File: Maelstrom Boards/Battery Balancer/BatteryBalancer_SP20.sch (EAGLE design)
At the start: 84 parts, among them IC3 REG1117, P2 39-30-16, Q1 SPB80P06P, Q10 MOSFET-NCH-AO3404A, Q11 MOSFET-NCH-AO3404A, Q19 FDD4141TO252, Q2 SPB80P06P, Q22 FDD4141TO252, Q3 NMOSFET-D2PAK-7, Q4 310mA/60V/1.6Ω, Q5 NMOSFET-D2PAK-7, Q6 FDD4141TO252, Q7 MOSFET-NCH-AO3404A, Q8 MOSFET-NCH-AO3404A, Q9 MOSFET-NCH-AO3404A

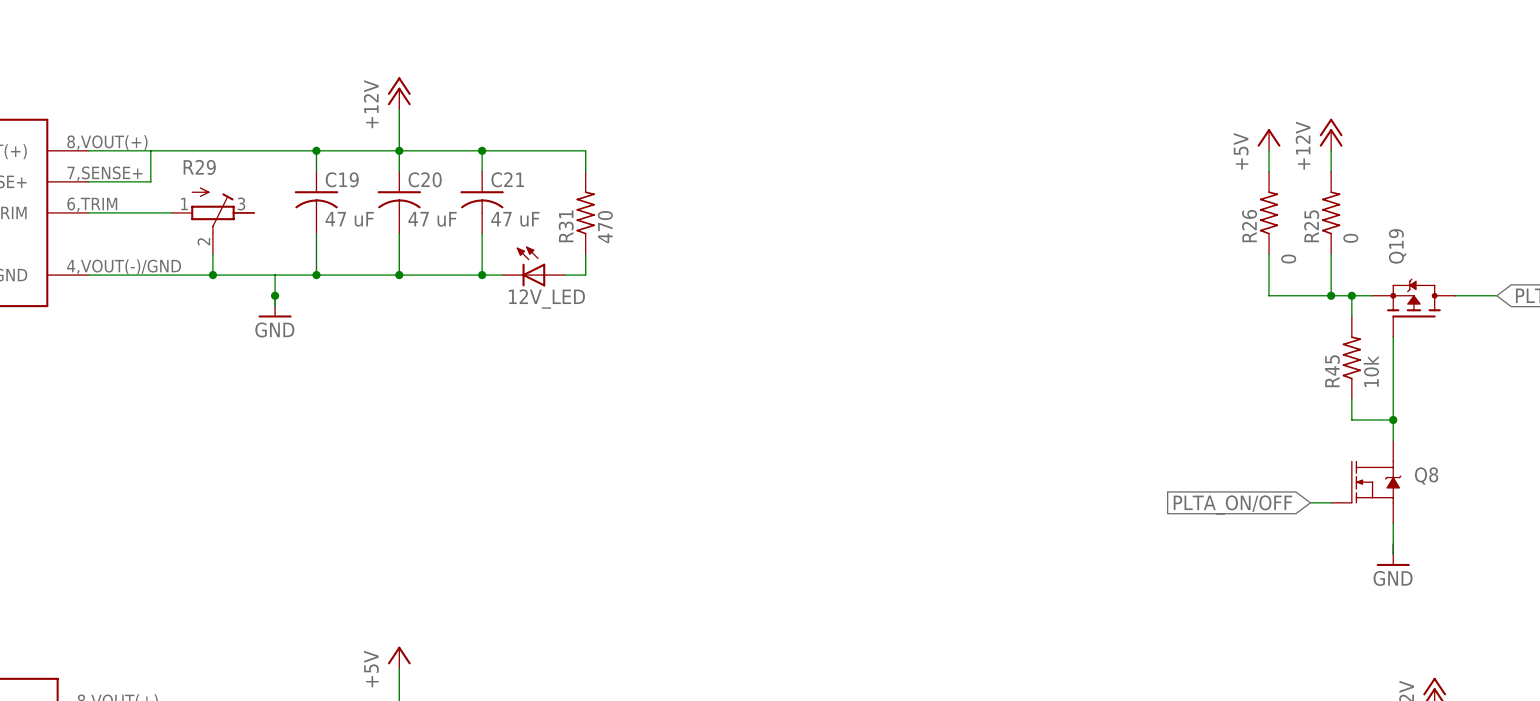
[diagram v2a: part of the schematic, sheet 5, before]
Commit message: Fixed review changes for Puddles BB
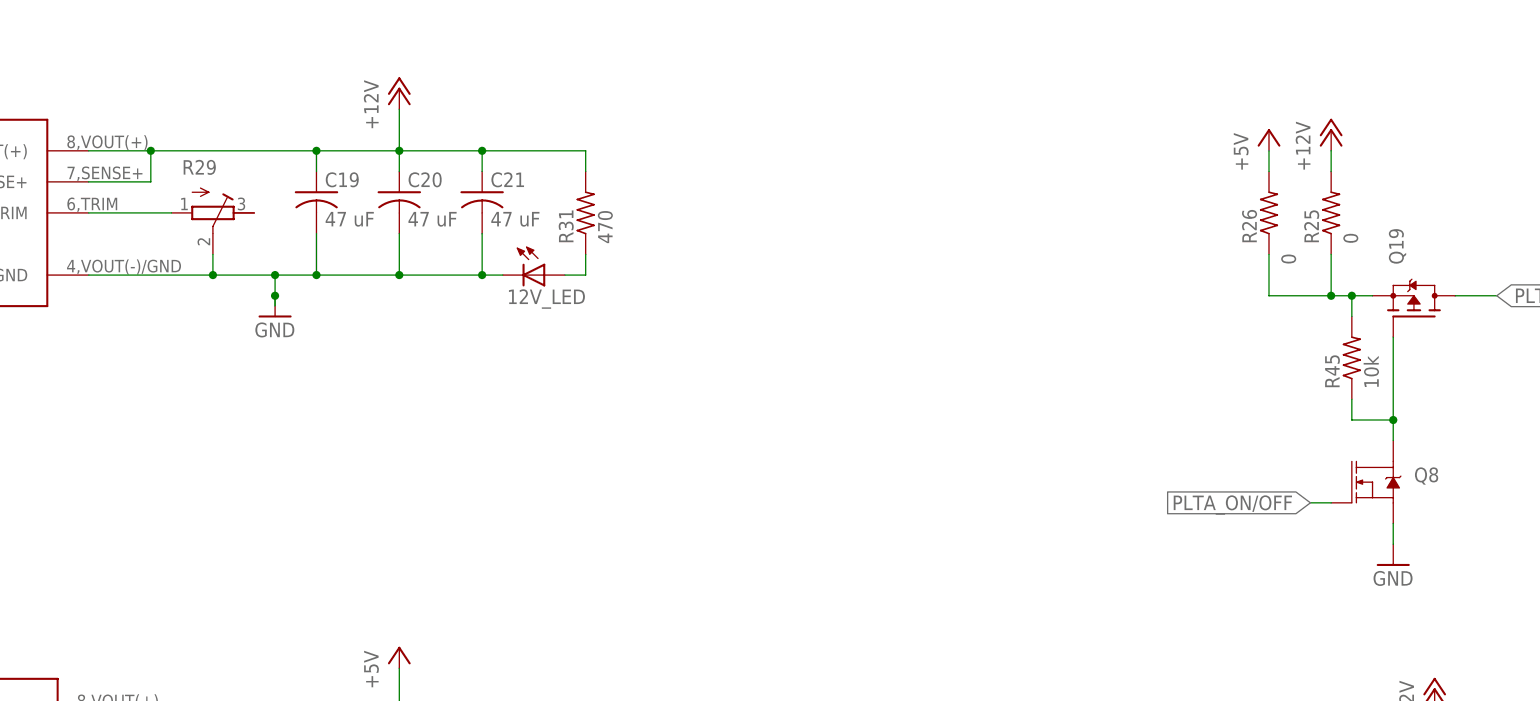
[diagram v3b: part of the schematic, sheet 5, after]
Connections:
- removed net GND1: U$5.1-
- net GND: now also U$5.1-
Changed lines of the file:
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@@
 <junction x="332.74" y="195.58"/>
 </segment>
+<segment>
+<pinref part="U$5" gate="G$1" pin="1-"/>
+<wire x1="88.9" y1="187.96" x2="91.44" y2="187.96" width="0.1524" layer="91"/>
+<pinref part="GND3" gate="1" pin="GND"/>
+</segment>
 </net>
 <net name="STBD_BATTERY" class="0">
@@
 </segment>
 </net>
-<net name="GND1" class="0">
-<segment>
-<wire x1="91.44" y1="187.96" x2="91.44" y2="185.42" width="0.1524" layer="91"/>
-<pinref part="U$5" gate="G$1" pin="1-"/>
-<wire x1="88.9" y1="187.96" x2="91.44" y2="187.96" width="0.1524" layer="91"/>
-<pinref part="GND3" gate="1" pin="GND"/>
-</segment>
-</net>
 <net name="MOTOR_POWER" class="0">
 <segment>
@@
 <pinref part="P+15" gate="1" pin="+12V"/>
 <wire x1="175.26" y1="228.6" x2="175.26" y2="233.68" width="0.1524" layer="91"/>
+<junction x="144.78" y="228.6"/>
 </segment>
 <segment>
@@
 <pinref part="GND19" gate="1" pin="GND"/>
 <junction x="160.02" y="210.82"/>
+<junction x="160.02" y="213.36"/>
 </segment>
 <segment>
@@
 </segment>
 </net>
-<net name="GND2" class="0">
-<segment>
-<wire x1="297.18" y1="179.07" x2="297.18" y2="180.34" width="0.1524" layer="91"/>
-</segment>
-</net>
